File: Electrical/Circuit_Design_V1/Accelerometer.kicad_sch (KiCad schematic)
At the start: 0 parts

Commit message: #3 Adding accelerometer to schematic.
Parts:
- added C11: 10uF, symbol Device:C
- added U2: ADXL343, Package_LGA:LGA-14_3x5mm_P0.8mm_LayoutBorder1x6y, symbol Sensor_Motion:ADXL343
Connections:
- new net +3V3: C11.2, U2.11 (RES), U2.2 (GND), U2.3 (RES), U2.4 (GND), U2.5 (GND), U2.6 (Vs)
- new net ADX_CS#: U2.7 (~{CS})
- new net ADX_INT1: U2.8 (INT1)
- new net ADX_INT2: U2.9 (INT2)
- new net ADX_SCLK: U2.14 (SCL/SCLK)
- new net ADX_SD0: U2.12 (SDO/ADDR)
- new net ADX_SDI: U2.13 (SDA/SDI/SDIO)
- new net GND: C11.1
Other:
- company: (none) -> AdrianTheHacker
- title: (none) -> Accelerometer

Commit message: #3 Improving accelerometer schematic.
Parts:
- added C13: 0.1uF, Capacitor_SMD:C_0805_2012Metric, symbol Device:C
- added R1: 1370Ω, Resistor_SMD:R_0805_2012Metric, symbol Device:R
- added R2: 1650Ω, Resistor_SMD:R_0805_2012Metric, symbol Device:R
- C11: value 10uF -> 1uF; footprint (none) -> Capacitor_SMD:C_0805_2012Metric; Digikey Part Number 3372-0603W106M6R3XDTR-ND -> 1276-1029-2-ND
- U2: Digikey Part Number 505-ADXL343BCCZ-RL7TR-ND -> (none)
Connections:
- net +3V3: now also R1.1; no longer U2.11 (RES), U2.2 (GND), U2.4 (GND), U2.5 (GND)
- net GND: now also U2.11 (RES), U2.2 (GND), U2.4 (GND), U2.5 (GND), C13.2, R2.1
- net at U2.1 (Vdd_I/O): now also C13.1, R1.2, R2.2
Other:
- moved on the sheet: C11

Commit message: #3 Finishing some circuitry.
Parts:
- C11: Digikey Part Number 1276-1029-2-ND -> 478-5265-1-ND
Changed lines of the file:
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@@
 			)
 		)
-		(property "Datasheet" "https://mm.digikey.com/Volume0/opasdata/d220001/medias/docus/609/CL21B105KBFNNNE_Spec.pdf"
+		(property "Datasheet" "https://datasheets.kyocera-avx.com/TLC.pdf"
 			(at 81.28 81.28 0)
 			(effects
@@
 			)
 		)
-		(property "Digikey Part Number" "1276-1029-2-ND"
+		(property "Digikey Part Number" "478-5265-1-ND"
 			(at 81.28 81.28 0)
 			(effects

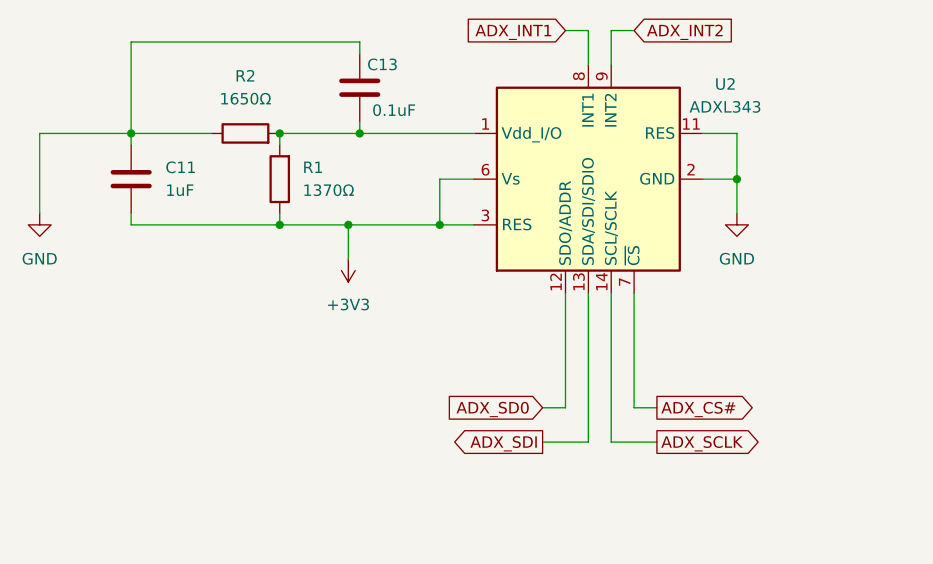
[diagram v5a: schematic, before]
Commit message: Completing schematic.
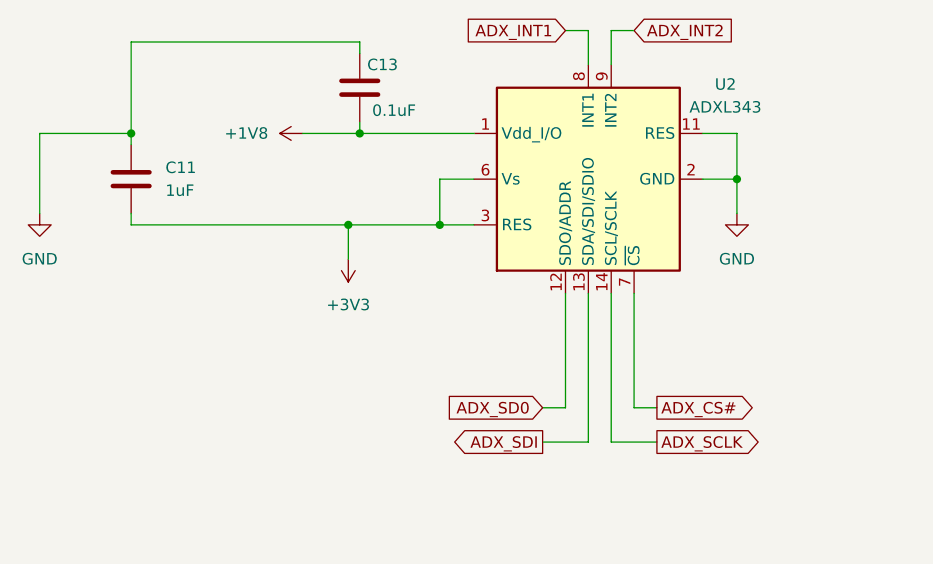
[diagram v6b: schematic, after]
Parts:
- removed R1: 1370Ω, Resistor_SMD:R_0805_2012Metric, symbol Device:R
- removed R2: 1650Ω, Resistor_SMD:R_0805_2012Metric, symbol Device:R
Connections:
- net +1V8: now reaches C13.1, U2.1 (Vdd_I/O)
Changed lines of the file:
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@@
-	)
-	(junction
-		(at 97.79 76.2)
-		(diameter 0)
-		(color 0 0 0 0)
-	)
-	(junction
-		(at 97.79 86.36)
-		(diameter 0)
-		(color 0 0 0 0)
 	)
 	(junction
@@
 	(wire
 		(pts
-			(xy 97.79 77.47) (xy 97.79 76.2)
+			(xy 100.33 76.2) (xy 106.68 76.2)
 		)
 		(stroke
@@
 	(wire
 		(pts
-			(xy 97.79 86.36) (xy 105.41 86.36)
+			(xy 81.28 86.36) (xy 105.41 86.36)
 		)
 		(stroke
@@
 	(wire
 		(pts
-			(xy 97.79 86.36) (xy 97.79 85.09)
-		)
-		(stroke
-			(width 0)
-			(type default)
-		)
-	)
-	(wire
-		(pts
-			(xy 97.79 76.2) (xy 106.68 76.2)
-		)
-		(stroke
-			(width 0)
-			(type default)
-		)
-	)
-	(wire
-		(pts
 			(xy 71.12 76.2) (xy 81.28 76.2)
 		)
@@
 	(wire
 		(pts
-			(xy 81.28 86.36) (xy 97.79 86.36)
-		)
-		(stroke
-			(width 0)
-			(type default)
-		)
-	)
-	(wire
-		(pts
 			(xy 115.57 81.28) (xy 115.57 86.36)
 		)
@@
 		(pts
 			(xy 132.08 64.77) (xy 129.54 64.77)
-		)
-		(stroke
-			(width 0)
-			(type default)
-		)
-	)
-	(wire
-		(pts
-			(xy 81.28 76.2) (xy 90.17 76.2)
 		)
 		(stroke
@@
 				(justify left)
 				(hide yes)
+			)
+		)
+	)
+	(symbol
+		(lib_id "power:+1V8")
+		(at 100.33 76.2 90)
+		(unit 1)
+		(exclude_from_sim no)
+		(in_bom yes)
+		(on_board yes)
+		(dnp no)
+		(fields_autoplaced yes)
+		(property "Reference" "#PWR032"
+			(at 104.14 76.2 0)
+			(effects
+				(font
+					(size 1.27 1.27)
+				)
+				(hide yes)
+			)
+		)
+		(property "Value" "+1V8"
+			(at 96.52 76.1999 90)
+			(effects
+				(font
+					(size 1.27 1.27)
+				)
+				(justify left)
+			)
+		)
+		(property "Footprint" ""
+			(at 100.33 76.2 0)
+			(effects
+				(font
+					(size 1.27 1.27)
+				)
+				(hide yes)
+			)
+		)
+		(property "Datasheet" ""
+			(at 100.33 76.2 0)
+			(effects
+				(font
+					(size 1.27 1.27)
+				)
+				(hide yes)
+			)
+		)
+		(property "Description" "Power symbol creates a global label with name \"+1V8\""
+			(at 100.33 76.2 0)
+			(effects
+				(font
+					(size 1.27 1.27)
+				)
+				(hide yes)
+			)
+		)
+		(pin "1"
+		)
+		(instances
+			(project "Circuit_Design_V1"
+				(path "/40e3562c-f358-42bb-8418-a7c96a575201/77ccf48f-6fc6-40d1-bcac-a7b0f3f18bd6"
+					(reference "#PWR032")
+					(unit 1)
+				)
 			)
 		)
@@
 				(path "/40e3562c-f358-42bb-8418-a7c96a575201/77ccf48f-6fc6-40d1-bcac-a7b0f3f18bd6"
 					(reference "C11")
-					(unit 1)
-				)
-			)
-		)
-	)
-	(symbol
-		(lib_id "Device:R")
-		(at 97.79 81.28 180)
-		(unit 1)
-		(exclude_from_sim no)
-		(in_bom yes)
-		(on_board yes)
-		(dnp no)
-		(property "Reference" "R1"
-			(at 100.33 80.0099 0)
-			(effects
-				(font
-					(size 1.27 1.27)
-				)
-				(justify right)
-			)
-		)
-		(property "Value" "1370Ω"
-			(at 100.33 82.5499 0)
-			(effects
-				(font
-					(size 1.27 1.27)
-				)
-				(justify right)
-			)
-		)
-		(property "Footprint" "Resistor_SMD:R_0805_2012Metric"
-			(at 99.568 81.28 90)
-			(effects
-				(font
-					(size 1.27 1.27)
-				)
-				(hide yes)
-			)
-		)
-		(property "Datasheet" "https://industrial.panasonic.com/cdbs/www-data/pdf/RDM0000/AOA0000C307.pdf"
-			(at 97.79 81.28 0)
-			(effects
-				(font
-					(size 1.27 1.27)
-				)
-				(hide yes)
-			)
-		)
-		(property "Description" "Resistor"
-			(at 97.79 81.28 0)
-			(effects
-				(font
-					(size 1.27 1.27)
-				)
-				(hide yes)
-			)
-		)
-		(property "Digikey Part Number" "P1.37KDATR-ND"
-			(at 97.79 81.28 0)
-			(effects
-				(font
-					(size 1.27 1.27)
-				)
-				(hide yes)
-			)
-		)
-		(pin "1"
-		)
-		(pin "2"
-		)
-		(instances
-			(project ""
-				(path "/40e3562c-f358-42bb-8418-a7c96a575201/77ccf48f-6fc6-40d1-bcac-a7b0f3f18bd6"
-					(reference "R1")
 					(unit 1)
 				)
@@
 					(unit 1)
 				)
-			)
-		)
-	)
-	(symbol
-		(lib_id "Device:R")
-		(at 93.98 76.2 90)
-		(unit 1)
-		(exclude_from_sim no)
-		(in_bom yes)
-		(on_board yes)
-		(dnp no)
-		(fields_autoplaced yes)
-		(property "Reference" "R2"
-			(at 93.98 69.85 90)
-			(effects
-				(font
-					(size 1.27 1.27)
-				)
-			)
-		)
-		(property "Value" "1650Ω"
-			(at 93.98 72.39 90)
-			(effects
-				(font
-					(size 1.27 1.27)
-				)
-			)
-		)
-		(property "Footprint" "Resistor_SMD:R_0805_2012Metric"
-			(at 93.98 77.978 90)
-			(effects
-				(font
-					(size 1.27 1.27)
-				)
-				(hide yes)
-			)
-		)
-		(property "Datasheet" "https://www.yageogroup.com/content/datasheet/asset/file/PYU-RC_GROUP_51_ROHS_L"
-			(at 93.98 76.2 0)
-			(effects
-				(font
-					(size 1.27 1.27)
-				)
-				(hide yes)
-			)
-		)
-		(property "Description" "Resistor"
-			(at 93.98 76.2 0)
-			(effects
-				(font
-					(size 1.27 1.27)
-				)
-				(hide yes)
-			)
-		)
-		(property "Digikey Part Number" "311-1.65KCRTR-ND"
-			(at 93.98 76.2 90)
-			(effects
-				(font
-					(size 1.27 1.27)
-				)
-				(hide yes)
-			)
-		)
-		(pin "1"
-		)
-		(pin "2"
-		)
-		(instances
-			(project "Circuit_Design_V1"
-				(path "/40e3562c-f358-42bb-8418-a7c96a575201/77ccf48f-6fc6-40d1-bcac-a7b0f3f18bd6"
-					(reference "R2")
-					(unit 1)
-				)
